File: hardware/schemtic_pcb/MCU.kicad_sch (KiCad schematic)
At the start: 29 parts, among them J6 Conn_01x06, J7 SW_&_LED, J8 Serial Console, J9 MCP9700, SW1 Reset, SW2 WiFi, U3 ESP32-WROOM-32, U4 LM1117-3.3, U5 ADS1115IDGS

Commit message: Bump schematic and PCB to version 3.0
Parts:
- removed D5: DNF, Diode_SMD:D_MELF, symbol Device:D_Zener
- removed R12: 0R, Resistor_SMD:R_0603_1608Metric_Pad0.98x0.95mm_HandSolder, symbol Device:R
- added C16: 0.1uf, Capacitor_SMD:C_0603_1608Metric_Pad1.08x0.95mm_HandSolder, symbol Device:C
- added D5: 3V9, Package_TO_SOT_SMD:SOT-23, symbol Device:D_Zener_Dual_CommonCathode_AAK_Split
- D4: footprint Diode_SMD:D_MELF -> Package_TO_SOT_SMD:SOT-23; symbol Device:D_Zener -> Device:D_Zener_Dual_CommonCathode_AAK_Split
- R11: value 2k2 -> 1k
- U3: footprint PJA_Modules:ESP32-WROOM-32 -> RF_Module:ESP32-WROOM-32
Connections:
- net BAT_VOLT_S is gone; now on net BAT+SENSE: J6.4 (Pin_4)
- net GND: now also D4.1 (A), C16.2, D5.1 (A); no longer D4.2 (A)
- net BAT+SENSE: now reaches C11.1, R11.1, U5.6 (AIN2)
- net BAT+SENSE: now also D4.3 (K); no longer D4.1 (K)
- net AMPS_SENSE- renamed BAT-SENSE
- net BAT-SENSE: now also C16.1, D5.3 (K)

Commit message: - Update ADC input protextion zenners from 3V9 to 4V7 volts - Fix unrouted track - Update PCB and schemtaic to v3.1
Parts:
- D4, D5: value 3V9 -> 4V7
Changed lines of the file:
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@@
   (paper "A4")
   (title_block
-    (rev "3.0")
+    (rev "3.1")
   )
   (junction (at 17.145 51.435) (diameter 0) (color 0 0 0 0)
@@
       (effects (font (size 1.27 1.27)) (justify left))
     )
-    (property "Value" "3V9" (id 1) (at 217.17 143.51 90)
+    (property "Value" "4V7" (id 1) (at 217.17 143.51 90)
       (effects (font (size 1.27 1.27)) (justify left))
     )
@@
       (effects (font (size 1.27 1.27)) (justify left))
     )
-    (property "Value" "3V9" (id 1) (at 236.22 143.51 90)
-      (effects (font (size 1.27 1.27)) (justify left))
-    )
+    (property "Value" "4V7" (id 1) (at 236.22 143.51 90)
+      (effects (font (size 1.27 1.27)) (justify left))
+    )

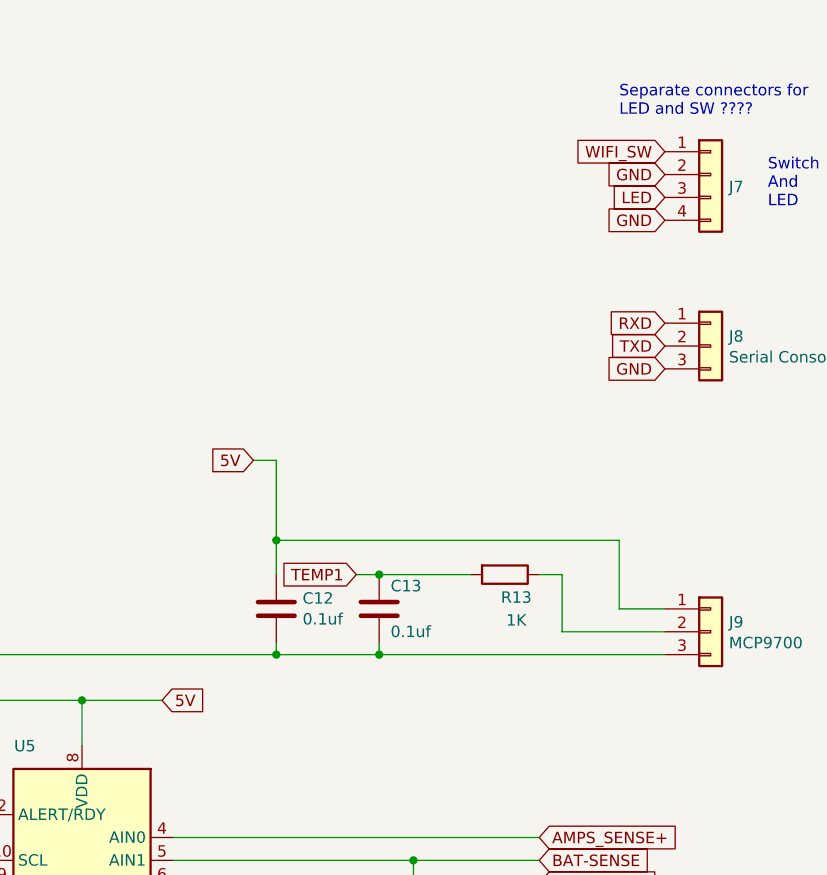
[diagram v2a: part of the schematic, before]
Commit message: Remove notes from schematic and pcb.
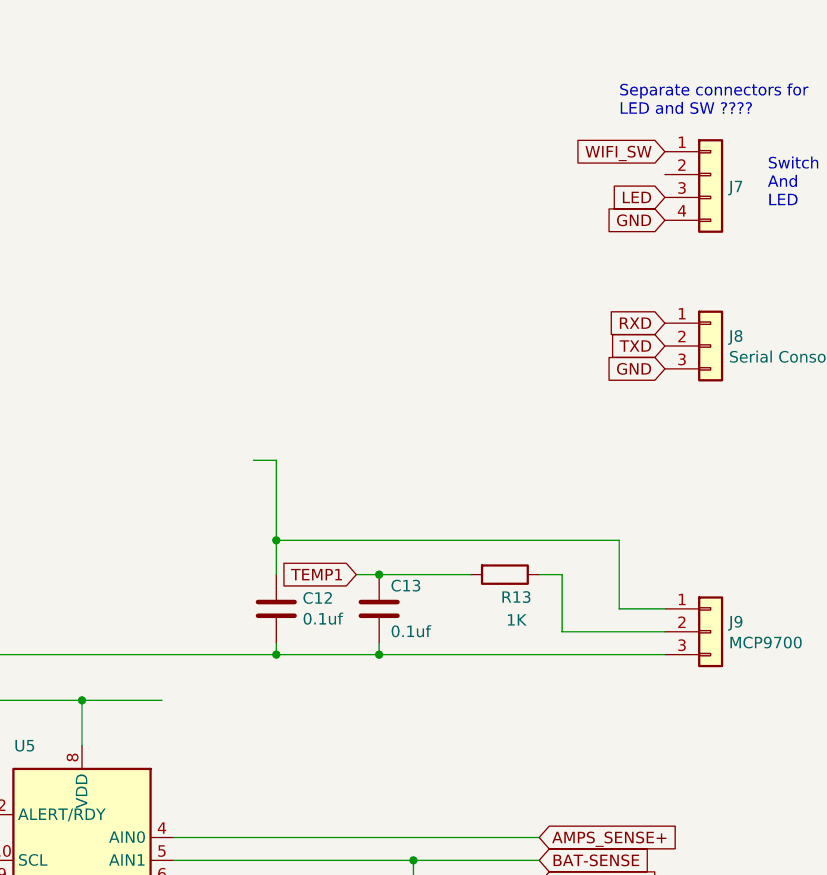
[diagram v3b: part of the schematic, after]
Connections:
- net 5V: no longer C10.1, C12.1, J9.1 (Pin_1), U5.8 (VDD)
- net GND: no longer J7.2 (Pin_2)
- new net: C12.1, J9.1 (Pin_1)
- new net: C10.1, U5.8 (VDD)
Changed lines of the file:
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@@
     )
-  )
-  (global_label "5V" (shape input) (at 194.31 104.14 0) (fields_autoplaced)
-    (effects (font (size 1.27 1.27)) (justify left))
-    (property "Intersheet References" "${INTERSHEET_REFS}" (id 0) (at 16.51 17.78 0))
   )
   (global_label "TXD" (shape input) (at 250.19 64.77 180) (fields_autoplaced)
@@
     (effects (font (size 1.27 1.27)) (justify left))
     (property "Intersheet References" "${INTERSHEET_REFS}" (id 0) (at 25.4 17.78 0))
-  )
-  (global_label "GND" (shape input) (at 250.19 45.72 180) (fields_autoplaced)
-    (effects (font (size 1.27 1.27)) (justify right))
-    (property "Intersheet References" "${INTERSHEET_REFS}" (id 0) (at 16.51 17.78 0))
   )
   (global_label "3V3" (shape input) (at 118.11 134.62 0) (fields_autoplaced)
@@
     (effects (font (size 1.27 1.27)) (justify right))
     (property "Intersheet References" "${INTERSHEET_REFS}" (id 0) (at 16.51 17.78 0))
-  )
-  (global_label "5V" (shape input) (at 204.47 77.47 180) (fields_autoplaced)
-    (effects (font (size 1.27 1.27)) (justify right))
-    (property "Intersheet References" "${INTERSHEET_REFS}" (id 0) (at 16.51 17.78 0))

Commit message: Add latest schematic and PCB.
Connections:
- net 5V: now also C10.1, C12.1, J9.1 (Pin_1), U5.8 (VDD)
- net GND: now also J7.2 (Pin_2)
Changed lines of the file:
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@@
     )
+  )
+  (global_label "5V" (shape input) (at 204.47 77.47 180) (fields_autoplaced)
+    (effects (font (size 1.27 1.27)) (justify right))
+    (property "Intersheet References" "${INTERSHEET_REFS}" (id 0) (at 16.51 17.78 0))
   )
   (global_label "TXD" (shape input) (at 250.19 64.77 180) (fields_autoplaced)
     (effects (font (size 1.27 1.27)) (justify right))
     (property "Intersheet References" "${INTERSHEET_REFS}" (id 0) (at 16.51 17.78 0))
+  )
+  (global_label "GND" (shape input) (at 250.19 45.72 180) (fields_autoplaced)
+    (effects (font (size 1.27 1.27)) (justify right))
+    (property "Intersheet References" "${INTERSHEET_REFS}" (id 0) (at 243.9953 45.7994 0)
+      (effects (font (size 1.27 1.27)) (justify right))
+    )
   )
   (global_label "TEMP1" (shape input) (at 204.47 127 0) (fields_autoplaced)
@@
     (property "Intersheet References" "${INTERSHEET_REFS}" (id 0) (at 16.51 17.78 0))
   )
+  (global_label "5V" (shape input) (at 194.31 104.14 0) (fields_autoplaced)
+    (effects (font (size 1.27 1.27)) (justify left))
+    (property "Intersheet References" "${INTERSHEET_REFS}" (id 0) (at 382.27 163.83 0))
+  )
   (global_label "BAT-SENSE" (shape input) (at 236.22 121.92 0) (fields_autoplaced)
